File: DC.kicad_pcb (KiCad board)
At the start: 4 copper layers, 199.5 x 140 mm, 107 parts, among them J1 348302001, J2 348302001, J3 757570141, J4 PPTC021LFBN-RC, Q1 BSS806NE, Q2 BSS806NE, Q3 BSS806NE, Q4 BSS806NE, Q5 BSS806NE, U1 MCP2551-I-P, U2 100DP6T1B1M1QEH, U5 NUCLEO-F302R8, U6 C1F 3

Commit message: hello
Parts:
- S1, S2, S3: value LP6OA2ASRG -> LP11EE1NCSYG; footprint DriverControlsLib:LP6OA2ASRG -> DriverControlsLib:LP11EE1NCSYG
- moved S2 4.60 mm to (145.5, 133.0)
- moved S3 4.53 mm to (93.5, 133.0)
- moved S1 4.42 mm to (120.2, 133.0)
- moved R17 1.27 mm to (101.0, 140.4)
- moved C4 1.27 mm to (101.0, 134.5)
- moved C2 0.12 mm to (127.0, 134.5)
- moved R15 0.12 mm to (127.0, 140.5)
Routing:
- net /LSignalLightIn: track 104.5 -> 108.3 mm
- net /RSignalLightIn: track 38.3 -> 41.6 mm
- net /HazardIn: track 74.3 -> 76.9 mm

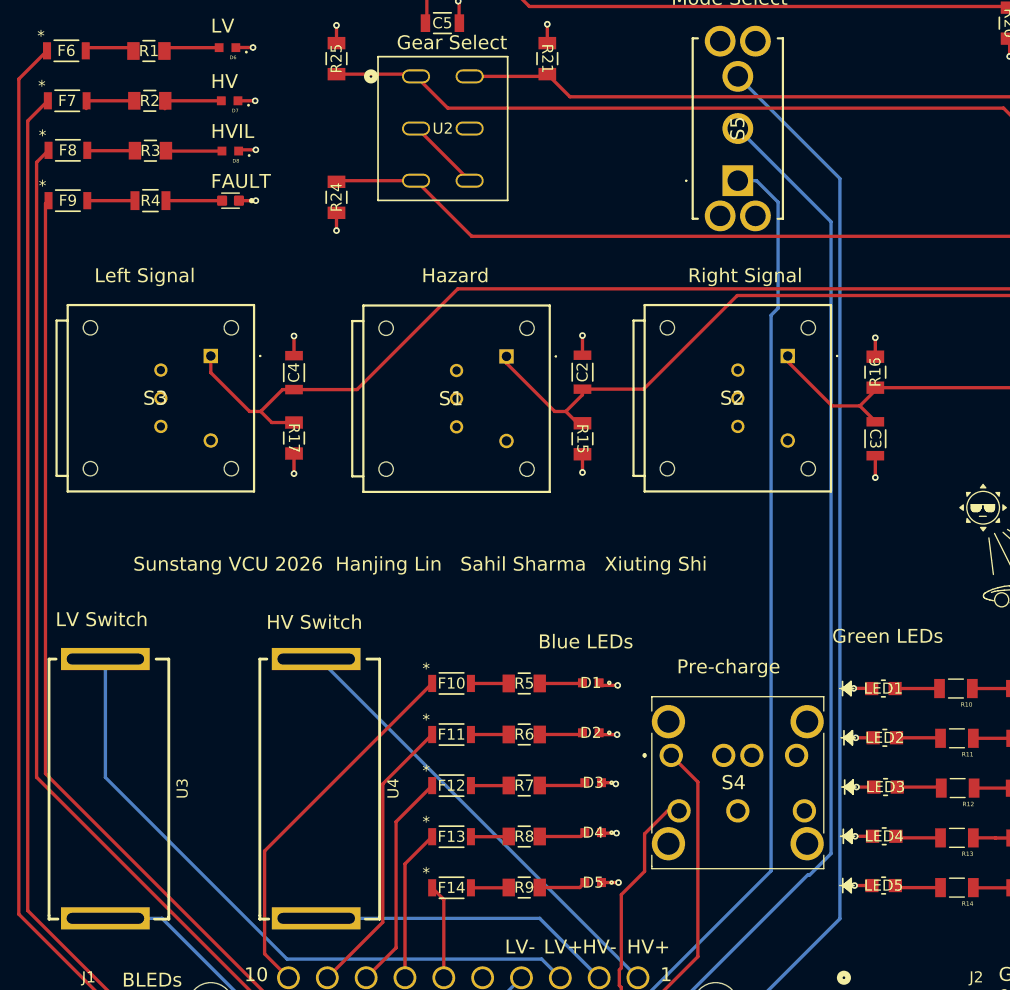
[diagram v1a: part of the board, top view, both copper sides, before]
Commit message: Changed pad size
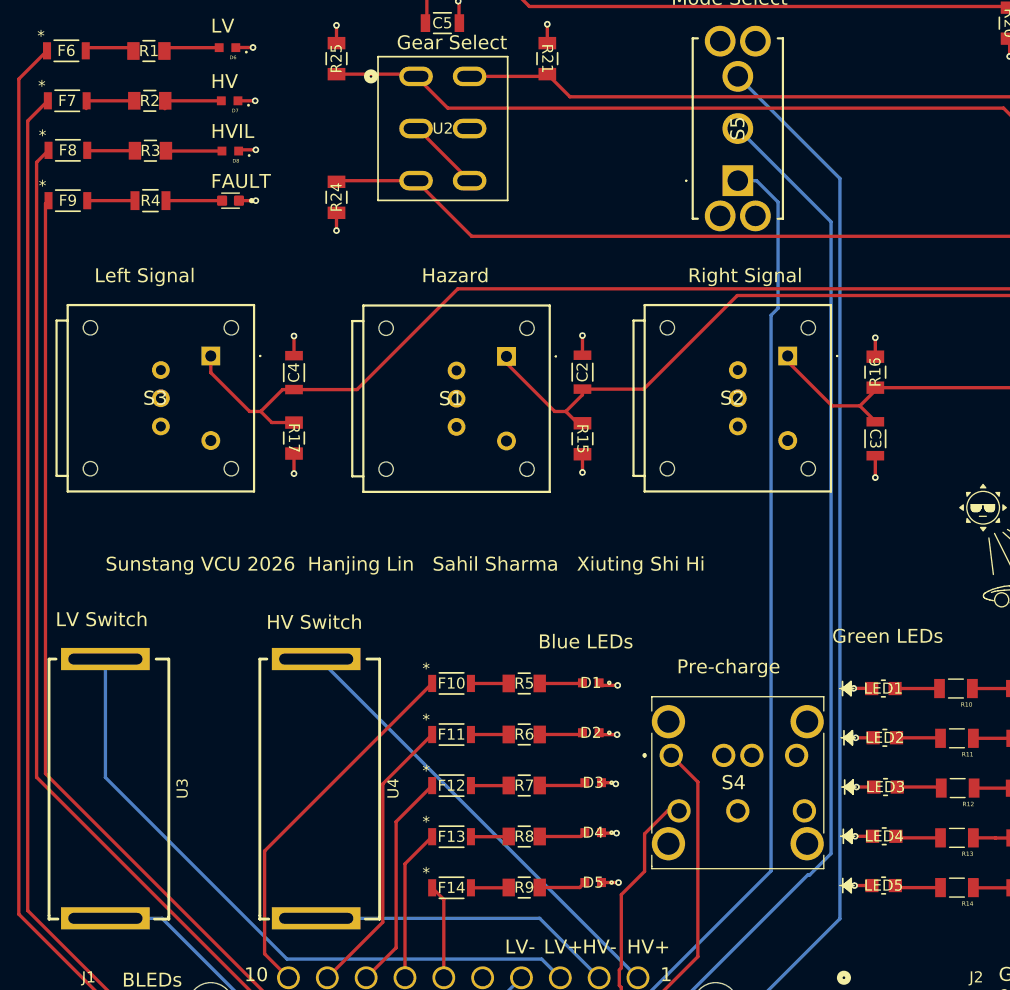
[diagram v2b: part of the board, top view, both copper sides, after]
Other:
- board text added: "Sunstang VCU 2026 Hanjing Lin Sahil Sharma Xiuting Shi Hi"
- board text removed: "Sunstang VCU 2026 Hanjing Lin Sahil Sharma Xiuting Shi"

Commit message: u
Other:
- board text added: "Sunstang VCU 2026 Hanjing Lin Sahil Sharma Xiuting Shi"
- board text removed: "Sunstang VCU 2026 Hanjing Lin Sahil Sharma Xiuting Shi Hi"
